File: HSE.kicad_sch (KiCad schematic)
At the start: 5 parts, among them Y1 25MHz

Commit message: ongoing add of MCU, etc.
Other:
- title: ADCs for 10K thermistors -> Multiplex I2C to Screw Terminal connectors
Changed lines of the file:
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@@
 	(paper "A4")
 	(title_block
-		(title "ADCs for 10K thermistors")
-		(date "2025-01-07")
-		(rev "v0.1.1")
+		(title "Multiplex I2C to Screw Terminal connectors")
+		(date "2025-09-07")
+		(rev "v0.2.0")
 	)
 	(junction
@@
 		(instances
 			(project ""
-				(path "/0c2d0c14-8850-4a30-bb78-b2f40cb442ba/f12d0b95-be3f-41e2-8b41-943aec5e1edf/09b28461-e1e3-4809-8d37-797a691b7cc0"
+				(path "/0c2d0c14-8850-4a30-bb78-b2f40cb442ba/2810e5bd-88e3-445e-9497-ea39bfab4c18/09b28461-e1e3-4809-8d37-797a691b7cc0"
 					(reference "#PWR03")
 					(unit 1)
@@
 		(instances
 			(project ""
-				(path "/0c2d0c14-8850-4a30-bb78-b2f40cb442ba/f12d0b95-be3f-41e2-8b41-943aec5e1edf/09b28461-e1e3-4809-8d37-797a691b7cc0"
+				(path "/0c2d0c14-8850-4a30-bb78-b2f40cb442ba/2810e5bd-88e3-445e-9497-ea39bfab4c18/09b28461-e1e3-4809-8d37-797a691b7cc0"
 					(reference "#PWR061")
 					(unit 1)
@@
 		(instances
 			(project "SensorProject_t16-pcb"
-				(path "/0c2d0c14-8850-4a30-bb78-b2f40cb442ba/f12d0b95-be3f-41e2-8b41-943aec5e1edf/09b28461-e1e3-4809-8d37-797a691b7cc0"
+				(path "/0c2d0c14-8850-4a30-bb78-b2f40cb442ba/2810e5bd-88e3-445e-9497-ea39bfab4c18/09b28461-e1e3-4809-8d37-797a691b7cc0"
 					(reference "C10")
 					(unit 1)
@@
 		(instances
 			(project "SensorProject_t16-pcb"
-				(path "/0c2d0c14-8850-4a30-bb78-b2f40cb442ba/f12d0b95-be3f-41e2-8b41-943aec5e1edf/09b28461-e1e3-4809-8d37-797a691b7cc0"
+				(path "/0c2d0c14-8850-4a30-bb78-b2f40cb442ba/2810e5bd-88e3-445e-9497-ea39bfab4c18/09b28461-e1e3-4809-8d37-797a691b7cc0"
 					(reference "R30")
 					(unit 1)
@@
 		(instances
 			(project ""
-				(path "/0c2d0c14-8850-4a30-bb78-b2f40cb442ba/f12d0b95-be3f-41e2-8b41-943aec5e1edf/09b28461-e1e3-4809-8d37-797a691b7cc0"
+				(path "/0c2d0c14-8850-4a30-bb78-b2f40cb442ba/2810e5bd-88e3-445e-9497-ea39bfab4c18/09b28461-e1e3-4809-8d37-797a691b7cc0"
 					(reference "#PWR060")
 					(unit 1)
@@
 		(instances
 			(project "SensorProject_t16-pcb"
-				(path "/0c2d0c14-8850-4a30-bb78-b2f40cb442ba/f12d0b95-be3f-41e2-8b41-943aec5e1edf/09b28461-e1e3-4809-8d37-797a691b7cc0"
+				(path "/0c2d0c14-8850-4a30-bb78-b2f40cb442ba/2810e5bd-88e3-445e-9497-ea39bfab4c18/09b28461-e1e3-4809-8d37-797a691b7cc0"
 					(reference "#PWR095")
 					(unit 1)
@@
 		(instances
 			(project ""
-				(path "/0c2d0c14-8850-4a30-bb78-b2f40cb442ba/f12d0b95-be3f-41e2-8b41-943aec5e1edf/09b28461-e1e3-4809-8d37-797a691b7cc0"
+				(path "/0c2d0c14-8850-4a30-bb78-b2f40cb442ba/2810e5bd-88e3-445e-9497-ea39bfab4c18/09b28461-e1e3-4809-8d37-797a691b7cc0"
 					(reference "Y1")
 					(unit 1)
@@
 		(instances
 			(project ""
-				(path "/0c2d0c14-8850-4a30-bb78-b2f40cb442ba/f12d0b95-be3f-41e2-8b41-943aec5e1edf/09b28461-e1e3-4809-8d37-797a691b7cc0"
+				(path "/0c2d0c14-8850-4a30-bb78-b2f40cb442ba/2810e5bd-88e3-445e-9497-ea39bfab4c18/09b28461-e1e3-4809-8d37-797a691b7cc0"
 					(reference "NT1")
 					(unit 1)
@@
 		(instances
 			(project "SensorProject_t16-pcb"
-				(path "/0c2d0c14-8850-4a30-bb78-b2f40cb442ba/f12d0b95-be3f-41e2-8b41-943aec5e1edf/09b28461-e1e3-4809-8d37-797a691b7cc0"
+				(path "/0c2d0c14-8850-4a30-bb78-b2f40cb442ba/2810e5bd-88e3-445e-9497-ea39bfab4c18/09b28461-e1e3-4809-8d37-797a691b7cc0"
 					(reference "C11")
 					(unit 1)

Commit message: symbols an footprints added for f411 change. ERC passes.
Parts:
- C10, C11: footprint ProjectLib:C_0402_1005Metric -> ProjectLib:C_0805_2012Metric
- R30: footprint ProjectLib:R_0402_1005Metric -> ProjectLib:R_0603_1608Metric
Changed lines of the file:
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@@
 		(on_board yes)
 		(dnp no)
-		(property "Reference" "#PWR061"
+		(property "Reference" "#PWR0111"
 			(at 142.24 88.9 0)
 			(effects
@@
 			(project ""
 				(path "/0c2d0c14-8850-4a30-bb78-b2f40cb442ba/2810e5bd-88e3-445e-9497-ea39bfab4c18/09b28461-e1e3-4809-8d37-797a691b7cc0"
-					(reference "#PWR061")
+					(reference "#PWR0111")
 					(unit 1)
 				)
@@
 			)
 		)
-		(property "Footprint" "ProjectLib:C_0402_1005Metric"
+		(property "Footprint" "ProjectLib:C_0805_2012Metric"
 			(at 153.9748 105.41 0)
 			(effects
@@
 			)
 		)
-		(property "Datasheet" ""
+		(property "Datasheet" "~"
 			(at 154.94 109.22 0)
 			(effects
@@
 			)
 		)
-		(property "Footprint" "ProjectLib:R_0402_1005Metric"
+		(property "Footprint" "ProjectLib:R_0603_1608Metric"
 			(at 155.956 82.804 90)
 			(effects
@@
 			)
 		)
-		(property "Datasheet" ""
+		(property "Datasheet" "~"
 			(at 154.94 82.55 0)
 			(effects
@@
 		(dnp no)
 		(fields_autoplaced yes)
-		(property "Reference" "#PWR060"
+		(property "Reference" "#PWR0112"
 			(at 138.43 132.08 0)
 			(effects
@@
 			(project ""
 				(path "/0c2d0c14-8850-4a30-bb78-b2f40cb442ba/2810e5bd-88e3-445e-9497-ea39bfab4c18/09b28461-e1e3-4809-8d37-797a691b7cc0"
-					(reference "#PWR060")
+					(reference "#PWR0112")
 					(unit 1)
 				)
@@
 			)
 		)
-		(property "Datasheet" "https://support.epson.biz/td/api/doc_check.php?dl=brief_FA-128&lang=en"
-			(at 147.32 93.98 0)
-			(effects
-				(font
-					(size 1.27 1.27)
-				)
-				(hide yes)
-			)
-		)
-		(property "Description" "Four pin crystal, GND on pins 2 and 4, 7pF"
+		(property "Datasheet" "~"
+			(at 147.32 93.98 0)
+			(effects
+				(font
+					(size 1.27 1.27)
+				)
+				(hide yes)
+			)
+		)
+		(property "Description" "Four pin crystal, GND on pins 2 and 4"
 			(at 147.32 93.98 0)
 			(effects
@@
 			)
 		)
-		(property "Footprint" "ProjectLib:C_0402_1005Metric"
+		(property "Footprint" "ProjectLib:C_0805_2012Metric"
 			(at 137.4648 105.41 0)
 			(effects
@@
 			)
 		)
-		(property "Datasheet" ""
+		(property "Datasheet" "~"
 			(at 138.43 109.22 0)
 			(effects

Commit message: ongoing
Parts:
- C10, C11: footprint ProjectLib:C_0805_2012Metric -> ProjectLib:C_0402_1005Metric
- R30: footprint ProjectLib:R_0603_1608Metric -> ProjectLib:R_0402_1005Metric
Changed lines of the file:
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@@
 			)
 		)
-		(property "Footprint" "ProjectLib:C_0805_2012Metric"
+		(property "Footprint" "ProjectLib:C_0402_1005Metric"
 			(at 153.9748 105.41 0)
 			(effects
@@
 			)
 		)
-		(property "Footprint" "ProjectLib:R_0603_1608Metric"
+		(property "Footprint" "ProjectLib:R_0402_1005Metric"
 			(at 155.956 82.804 90)
 			(effects
@@
 			)
 		)
-		(property "Footprint" "ProjectLib:C_0805_2012Metric"
+		(property "Footprint" "ProjectLib:C_0402_1005Metric"
 			(at 137.4648 105.41 0)
 			(effects

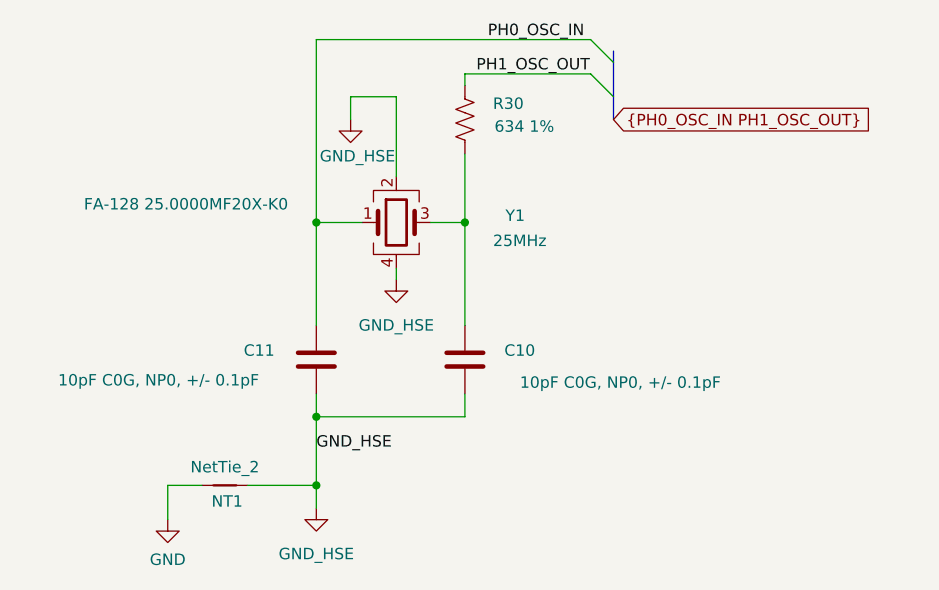
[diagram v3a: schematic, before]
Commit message: adding MCU, ongoing.
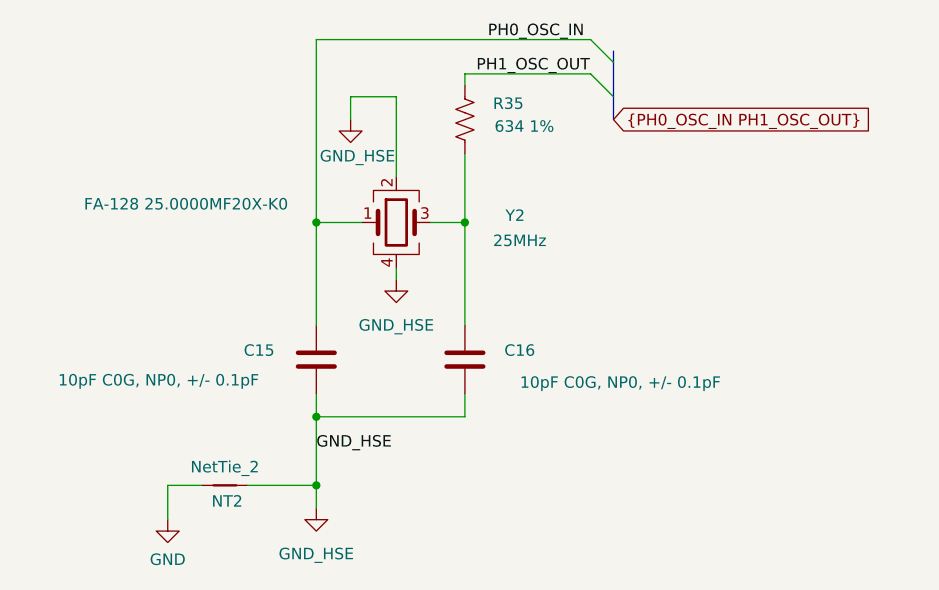
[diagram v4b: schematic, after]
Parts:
- renumbered C11 to C15, C10 to C16, NT1 to NT2, R30 to R35, Y1 to Y2
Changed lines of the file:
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@@
 		(dnp no)
 		(fields_autoplaced yes)
-		(property "Reference" "#PWR03"
+		(property "Reference" "#PWR070"
 			(at 147.32 106.68 0)
 			(effects
@@
 			(project ""
 				(path "/0c2d0c14-8850-4a30-bb78-b2f40cb442ba/2810e5bd-88e3-445e-9497-ea39bfab4c18/09b28461-e1e3-4809-8d37-797a691b7cc0"
-					(reference "#PWR03")
+					(reference "#PWR070")
 					(unit 1)
 				)
@@
 		(on_board yes)
 		(dnp no)
-		(property "Reference" "#PWR0111"
+		(property "Reference" "#PWR069"
 			(at 142.24 88.9 0)
 			(effects
@@
 			(project ""
 				(path "/0c2d0c14-8850-4a30-bb78-b2f40cb442ba/2810e5bd-88e3-445e-9497-ea39bfab4c18/09b28461-e1e3-4809-8d37-797a691b7cc0"
-					(reference "#PWR0111")
+					(reference "#PWR069")
 					(unit 1)
 				)
@@
 		(on_board yes)
 		(dnp no)
-		(property "Reference" "C10"
+		(property "Reference" "C16"
 			(at 161.036 108.204 0)
 			(effects
@@
 			(project "SensorProject_t16-pcb"
 				(path "/0c2d0c14-8850-4a30-bb78-b2f40cb442ba/2810e5bd-88e3-445e-9497-ea39bfab4c18/09b28461-e1e3-4809-8d37-797a691b7cc0"
-					(reference "C10")
+					(reference "C16")
 					(unit 1)
 				)
@@
 		(on_board yes)
 		(dnp no)
-		(property "Reference" "R30"
+		(property "Reference" "R35"
 			(at 159.766 80.772 0)
 			(effects
@@
 			(project "SensorProject_t16-pcb"
 				(path "/0c2d0c14-8850-4a30-bb78-b2f40cb442ba/2810e5bd-88e3-445e-9497-ea39bfab4c18/09b28461-e1e3-4809-8d37-797a691b7cc0"
-					(reference "R30")
+					(reference "R35")
 					(unit 1)
 				)
@@
 		(dnp no)
 		(fields_autoplaced yes)
-		(property "Reference" "#PWR0112"
+		(property "Reference" "#PWR068"
 			(at 138.43 132.08 0)
 			(effects
@@
 			(project ""
 				(path "/0c2d0c14-8850-4a30-bb78-b2f40cb442ba/2810e5bd-88e3-445e-9497-ea39bfab4c18/09b28461-e1e3-4809-8d37-797a691b7cc0"
-					(reference "#PWR0112")
+					(reference "#PWR068")
 					(unit 1)
 				)
@@
 		(dnp no)
 		(fields_autoplaced yes)
-		(property "Reference" "#PWR095"
+		(property "Reference" "#PWR067"
 			(at 121.92 133.35 0)
 			(effects
@@
 			(project "SensorProject_t16-pcb"
 				(path "/0c2d0c14-8850-4a30-bb78-b2f40cb442ba/2810e5bd-88e3-445e-9497-ea39bfab4c18/09b28461-e1e3-4809-8d37-797a691b7cc0"
-					(reference "#PWR095")
+					(reference "#PWR067")
 					(unit 1)
 				)
@@
 		(on_board yes)
 		(dnp no)
-		(property "Reference" "Y1"
+		(property "Reference" "Y2"
 			(at 160.528 93.218 0)
 			(effects
@@
 			(project ""
 				(path "/0c2d0c14-8850-4a30-bb78-b2f40cb442ba/2810e5bd-88e3-445e-9497-ea39bfab4c18/09b28461-e1e3-4809-8d37-797a691b7cc0"
-					(reference "Y1")
+					(reference "Y2")
 					(unit 1)
 				)
@@
 		(on_board yes)
 		(dnp no)
-		(property "Reference" "NT1"
+		(property "Reference" "NT2"
 			(at 128.524 124.968 0)
 			(effects
@@
 			(project ""
 				(path "/0c2d0c14-8850-4a30-bb78-b2f40cb442ba/2810e5bd-88e3-445e-9497-ea39bfab4c18/09b28461-e1e3-4809-8d37-797a691b7cc0"
-					(reference "NT1")
+					(reference "NT2")
 					(unit 1)
 				)
@@
 		(on_board yes)
 		(dnp no)
-		(property "Reference" "C11"
+		(property "Reference" "C15"
 			(at 132.08 108.204 0)
 			(effects
@@
 			(project "SensorProject_t16-pcb"
 				(path "/0c2d0c14-8850-4a30-bb78-b2f40cb442ba/2810e5bd-88e3-445e-9497-ea39bfab4c18/09b28461-e1e3-4809-8d37-797a691b7cc0"
-					(reference "C11")
+					(reference "C15")
 					(unit 1)
 				)

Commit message: ongoing.
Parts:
- renumbered C16 to C?, C15 to C?, NT2 to NT?, R35 to R?, Y2 to Y?
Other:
- title: Multiplex I2C to Screw Terminal connectors -> HSE
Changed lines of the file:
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@@
 	(paper "A4")
 	(title_block
-		(title "Multiplex I2C to Screw Terminal connectors")
-		(date "2025-09-07")
-		(rev "v0.2.0")
+		(title "HSE")
+		(date "2025-09-15")
+		(rev "v0.2.2")
 	)
 	(junction
@@
 		(dnp no)
 		(fields_autoplaced yes)
-		(property "Reference" "#PWR070"
+		(property "Reference" "#PWR?"
 			(at 147.32 106.68 0)
 			(effects
@@
 		)
 		(instances
-			(project ""
+			(project "multiplexI2C"
 				(path "/0c2d0c14-8850-4a30-bb78-b2f40cb442ba/2810e5bd-88e3-445e-9497-ea39bfab4c18/09b28461-e1e3-4809-8d37-797a691b7cc0"
-					(reference "#PWR070")
+					(reference "#PWR?")
 					(unit 1)
 				)
@@
 		(on_board yes)
 		(dnp no)
-		(property "Reference" "#PWR069"
+		(property "Reference" "#PWR?"
 			(at 142.24 88.9 0)
 			(effects
@@
 		)
 		(instances
-			(project ""
+			(project "multiplexI2C"
 				(path "/0c2d0c14-8850-4a30-bb78-b2f40cb442ba/2810e5bd-88e3-445e-9497-ea39bfab4c18/09b28461-e1e3-4809-8d37-797a691b7cc0"
-					(reference "#PWR069")
+					(reference "#PWR?")
 					(unit 1)
 				)
@@
 		(on_board yes)
 		(dnp no)
-		(property "Reference" "C16"
+		(property "Reference" "C?"
 			(at 161.036 108.204 0)
 			(effects
@@
 			)
 		)
-		(property "Datasheet" "~"
+		(property "Datasheet" ""
 			(at 154.94 109.22 0)
 			(effects
@@
 		)
 		(instances
-			(project "SensorProject_t16-pcb"
+			(project "multiplexI2C"
 				(path "/0c2d0c14-8850-4a30-bb78-b2f40cb442ba/2810e5bd-88e3-445e-9497-ea39bfab4c18/09b28461-e1e3-4809-8d37-797a691b7cc0"
-					(reference "C16")
+					(reference "C?")
 					(unit 1)
 				)
@@
 		(on_board yes)
 		(dnp no)
-		(property "Reference" "R35"
+		(property "Reference" "R?"
 			(at 159.766 80.772 0)
 			(effects
@@
 			)
 		)
-		(property "Datasheet" "~"
+		(property "Datasheet" ""
 			(at 154.94 82.55 0)
 			(effects
@@
 		)
 		(instances
-			(project "SensorProject_t16-pcb"
+			(project "multiplexI2C"
 				(path "/0c2d0c14-8850-4a30-bb78-b2f40cb442ba/2810e5bd-88e3-445e-9497-ea39bfab4c18/09b28461-e1e3-4809-8d37-797a691b7cc0"
-					(reference "R35")
+					(reference "R?")
 					(unit 1)
 				)
@@
 		(dnp no)
 		(fields_autoplaced yes)
-		(property "Reference" "#PWR068"
+		(property "Reference" "#PWR?"
 			(at 138.43 132.08 0)
 			(effects
@@
 		)
 		(instances
-			(project ""
+			(project "multiplexI2C"
 				(path "/0c2d0c14-8850-4a30-bb78-b2f40cb442ba/2810e5bd-88e3-445e-9497-ea39bfab4c18/09b28461-e1e3-4809-8d37-797a691b7cc0"
-					(reference "#PWR068")
+					(reference "#PWR?")
 					(unit 1)
 				)
@@
 		(dnp no)
 		(fields_autoplaced yes)
-		(property "Reference" "#PWR067"
+		(property "Reference" "#PWR?"
 			(at 121.92 133.35 0)
 			(effects
@@
 		)
 		(instances
-			(project "SensorProject_t16-pcb"
+			(project "multiplexI2C"
 				(path "/0c2d0c14-8850-4a30-bb78-b2f40cb442ba/2810e5bd-88e3-445e-9497-ea39bfab4c18/09b28461-e1e3-4809-8d37-797a691b7cc0"
-					(reference "#PWR067")
+					(reference "#PWR?")
 					(unit 1)
 				)
@@
 		(on_board yes)
 		(dnp no)
-		(property "Reference" "Y2"
+		(property "Reference" "Y?"
 			(at 160.528 93.218 0)
 			(effects
@@
 			)
 		)
-		(property "Datasheet" "~"
+		(property "Datasheet" "https://support.epson.biz/td/api/doc_check.php?dl=brief_FA-128&lang=en"
 			(at 147.32 93.98 0)
 			(effects
@@
 			)
 		)
-		(property "Description" "Four pin crystal, GND on pins 2 and 4"
+		(property "Description" "Four pin crystal, GND on pins 2 and 4, 7pF"
 			(at 147.32 93.98 0)
 			(effects
@@
 		)
 		(instances
-			(project ""
+			(project "multiplexI2C"
 				(path "/0c2d0c14-8850-4a30-bb78-b2f40cb442ba/2810e5bd-88e3-445e-9497-ea39bfab4c18/09b28461-e1e3-4809-8d37-797a691b7cc0"
-					(reference "Y2")
+					(reference "Y?")
 					(unit 1)
 				)
@@
 		(on_board yes)
 		(dnp no)
-		(property "Reference" "NT2"
+		(property "Reference" "NT?"
 			(at 128.524 124.968 0)
 			(effects
@@
 		)
 		(instances
-			(project ""
+			(project "multiplexI2C"
 				(path "/0c2d0c14-8850-4a30-bb78-b2f40cb442ba/2810e5bd-88e3-445e-9497-ea39bfab4c18/09b28461-e1e3-4809-8d37-797a691b7cc0"
-					(reference "NT2")
+					(reference "NT?")
 					(unit 1)
 				)
@@
 		(on_board yes)
 		(dnp no)
-		(property "Reference" "C15"
+		(property "Reference" "C?"
 			(at 132.08 108.204 0)
 			(effects
@@
 			)
 		)
-		(property "Datasheet" "~"
+		(property "Datasheet" ""
 			(at 138.43 109.22 0)
 			(effects
@@
 		)
 		(instances
-			(project "SensorProject_t16-pcb"
+			(project "multiplexI2C"
 				(path "/0c2d0c14-8850-4a30-bb78-b2f40cb442ba/2810e5bd-88e3-445e-9497-ea39bfab4c18/09b28461-e1e3-4809-8d37-797a691b7cc0"
-					(reference "C15")
+					(reference "C?")
 					(unit 1)
 				)

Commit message: ongoing.
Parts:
- gave numbers to parts that had none: 5
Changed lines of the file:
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@@
 		(dnp no)
 		(fields_autoplaced yes)
-		(property "Reference" "#PWR?"
+		(property "Reference" "#PWR0602"
 			(at 147.32 106.68 0)
 			(effects
@@
 			(project "multiplexI2C"
 				(path "/0c2d0c14-8850-4a30-bb78-b2f40cb442ba/2810e5bd-88e3-445e-9497-ea39bfab4c18/09b28461-e1e3-4809-8d37-797a691b7cc0"
-					(reference "#PWR?")
+					(reference "#PWR0602")
 					(unit 1)
 				)
@@
 		(on_board yes)
 		(dnp no)
-		(property "Reference" "#PWR?"
+		(property "Reference" "#PWR0601"
 			(at 142.24 88.9 0)
 			(effects
@@
 			(project "multiplexI2C"
 				(path "/0c2d0c14-8850-4a30-bb78-b2f40cb442ba/2810e5bd-88e3-445e-9497-ea39bfab4c18/09b28461-e1e3-4809-8d37-797a691b7cc0"
-					(reference "#PWR?")
+					(reference "#PWR0601")
 					(unit 1)
 				)
@@
 		(on_board yes)
 		(dnp no)
-		(property "Reference" "C?"
+		(property "Reference" "C602"
 			(at 161.036 108.204 0)
 			(effects
@@
 			(project "multiplexI2C"
 				(path "/0c2d0c14-8850-4a30-bb78-b2f40cb442ba/2810e5bd-88e3-445e-9497-ea39bfab4c18/09b28461-e1e3-4809-8d37-797a691b7cc0"
-					(reference "C?")
+					(reference "C602")
 					(unit 1)
 				)
@@
 		(on_board yes)
 		(dnp no)
-		(property "Reference" "R?"
+		(property "Reference" "R601"
 			(at 159.766 80.772 0)
 			(effects
@@
 			(project "multiplexI2C"
 				(path "/0c2d0c14-8850-4a30-bb78-b2f40cb442ba/2810e5bd-88e3-445e-9497-ea39bfab4c18/09b28461-e1e3-4809-8d37-797a691b7cc0"
-					(reference "R?")
+					(reference "R601")
 					(unit 1)
 				)
@@
 		(dnp no)
 		(fields_autoplaced yes)
-		(property "Reference" "#PWR?"
+		(property "Reference" "#PWR0603"
 			(at 138.43 132.08 0)
 			(effects
@@
 			(project "multiplexI2C"
 				(path "/0c2d0c14-8850-4a30-bb78-b2f40cb442ba/2810e5bd-88e3-445e-9497-ea39bfab4c18/09b28461-e1e3-4809-8d37-797a691b7cc0"
-					(reference "#PWR?")
+					(reference "#PWR0603")
 					(unit 1)
 				)
@@
 		(dnp no)
 		(fields_autoplaced yes)
-		(property "Reference" "#PWR?"
+		(property "Reference" "#PWR0604"
 			(at 121.92 133.35 0)
 			(effects
@@
 			(project "multiplexI2C"
 				(path "/0c2d0c14-8850-4a30-bb78-b2f40cb442ba/2810e5bd-88e3-445e-9497-ea39bfab4c18/09b28461-e1e3-4809-8d37-797a691b7cc0"
-					(reference "#PWR?")
+					(reference "#PWR0604")
 					(unit 1)
 				)
@@
 		(on_board yes)
 		(dnp no)
-		(property "Reference" "Y?"
+		(property "Reference" "Y601"
 			(at 160.528 93.218 0)
 			(effects
@@
 			(project "multiplexI2C"
 				(path "/0c2d0c14-8850-4a30-bb78-b2f40cb442ba/2810e5bd-88e3-445e-9497-ea39bfab4c18/09b28461-e1e3-4809-8d37-797a691b7cc0"
-					(reference "Y?")
+					(reference "Y601")
 					(unit 1)
 				)
@@
 		(on_board yes)
 		(dnp no)
-		(property "Reference" "NT?"
+		(property "Reference" "NT601"
 			(at 128.524 124.968 0)
 			(effects
@@
 			(project "multiplexI2C"
 				(path "/0c2d0c14-8850-4a30-bb78-b2f40cb442ba/2810e5bd-88e3-445e-9497-ea39bfab4c18/09b28461-e1e3-4809-8d37-797a691b7cc0"
-					(reference "NT?")
+					(reference "NT601")
 					(unit 1)
 				)
@@
 		(on_board yes)
 		(dnp no)
-		(property "Reference" "C?"
+		(property "Reference" "C601"
 			(at 132.08 108.204 0)
 			(effects
@@
 			(project "multiplexI2C"
 				(path "/0c2d0c14-8850-4a30-bb78-b2f40cb442ba/2810e5bd-88e3-445e-9497-ea39bfab4c18/09b28461-e1e3-4809-8d37-797a691b7cc0"
-					(reference "C?")
+					(reference "C601")
 					(unit 1)
 				)
